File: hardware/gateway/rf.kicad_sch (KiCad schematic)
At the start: 2 parts, among them IC2 CC1101RGPR

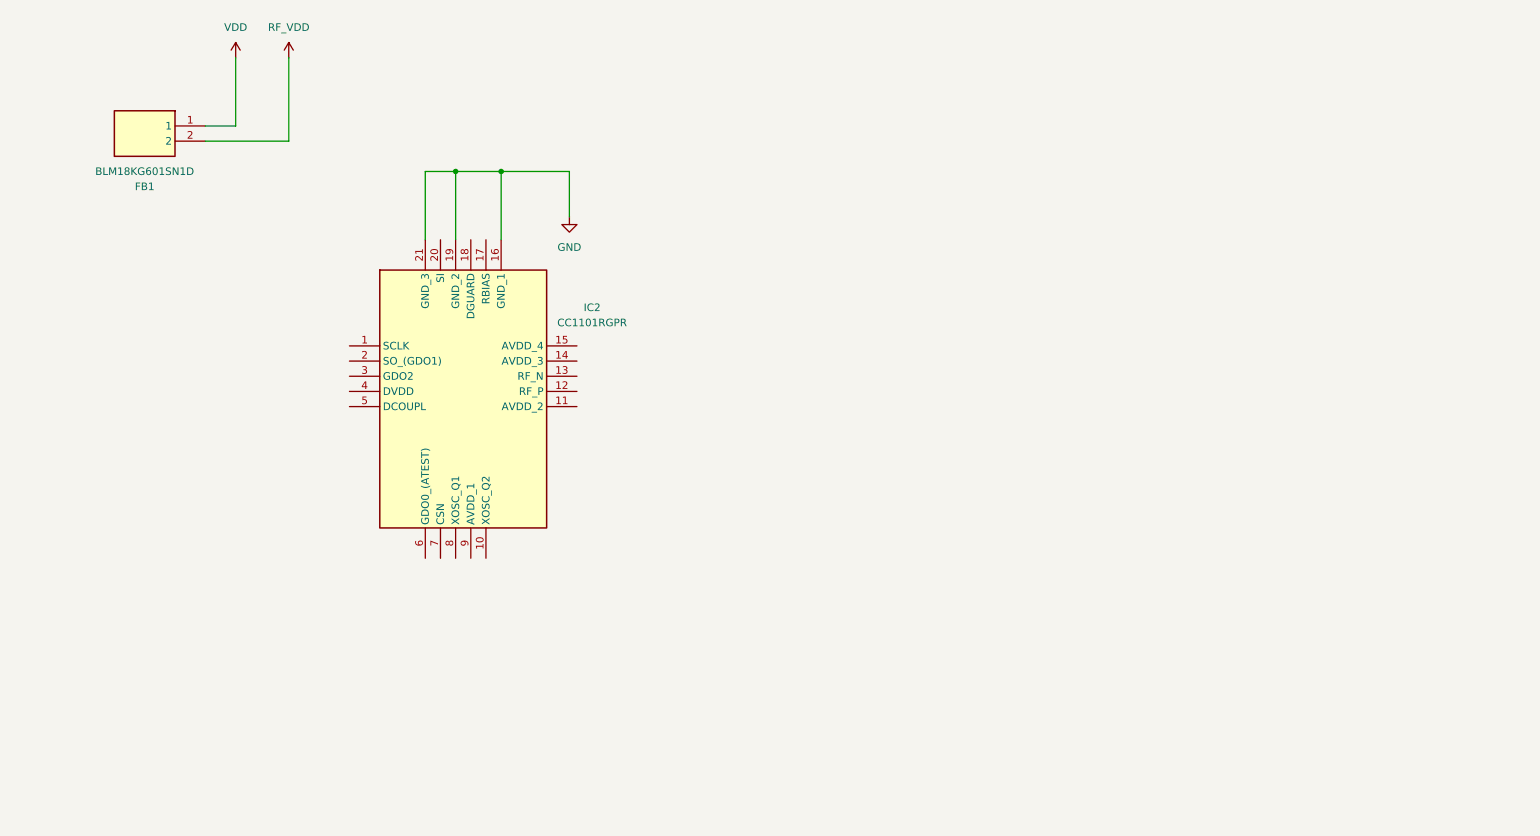
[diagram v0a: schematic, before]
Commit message: EG-11 All components connected in all sheets. The MCU pin mapping needs to be fixed. The BOM needs to be created. The FRAM need needs to be assessed.
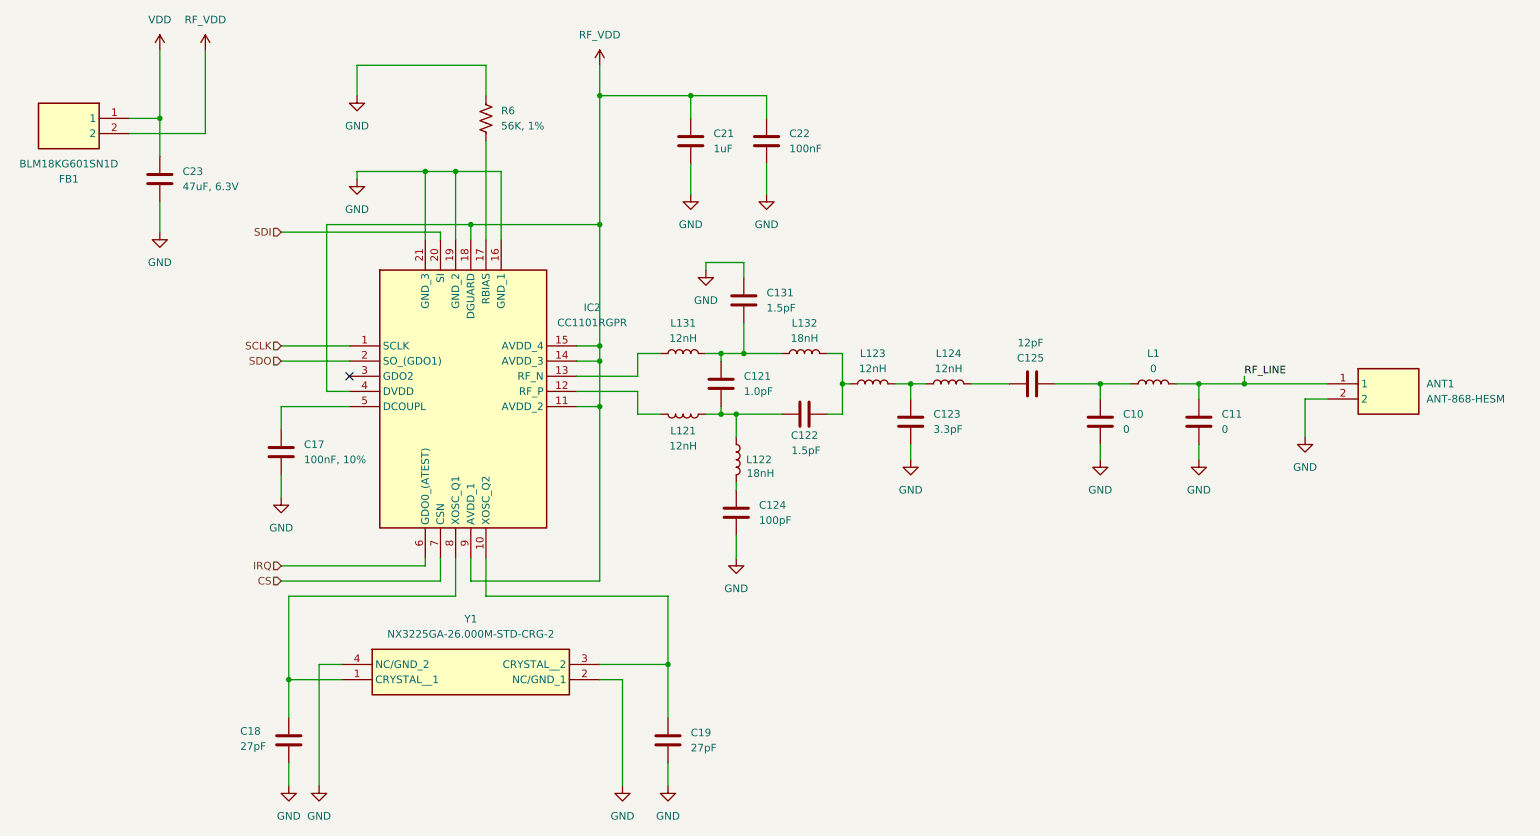
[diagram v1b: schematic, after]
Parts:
- added ANT1: ANT-868-HESM, MyParts:ANT-868-HESM, symbol ANT-868-HESM:ANT-868-HESM
- added C10, C11: 0, symbol Device:C
- added C121: 1.0pF, symbol Device:C
- added C122, C131: 1.5pF, symbol Device:C
- added C123: 3.3pF, symbol Device:C
- added C124: 100pF, symbol Device:C
- added C125: 12pF, symbol Device:C
- added C17: 100nF, 10%, symbol Device:C
- added C18, C19: 27pF, symbol Device:C
- added C21: 1uF, Capacitor_SMD:C_0603_1608Metric, symbol Device:C
- added C22: 100nF, Capacitor_SMD:C_0603_1608Metric, symbol Device:C
- added C23: 47uF, 6.3V, Capacitor_SMD:C_1206_3216Metric, symbol Device:C
- added L1: 0, symbol Device:L
- added L121, L123, L124, L131: 12nH, symbol Device:L
- added L122, L132: 18nH, symbol Device:L
- added R6: 56K, 1%, symbol Device:R_US
- added Y1: NX3225GA-26.000M-STD-CRG-2, MyParts:NX3225GA26000MSTDCRG2, symbol NX3225GA-26_000M-STD-CRG-2:NX3225GA-26.000M-STD-CRG-2
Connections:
- net GND: now also ANT1.2, C10.2, C11.2, C123.2, C124.2, C131.1, C17.2, C18.2, C19.2, C21.2, C22.2, C23.2, R6.1, Y1.2 (NC/GND_1), Y1.4 (NC/GND_2)
- net RF_VDD: now also IC2.11 (AVDD_2), IC2.14 (AVDD_3), IC2.15 (AVDD_4), IC2.18 (DGUARD), IC2.4 (DVDD), IC2.9 (AVDD_1), C21.1, C22.1
- net VDD: now also C23.1
- net SCLK: now reaches IC2.1 (SCLK)
- net at IC2.10 (XOSC_Q2): now also C19.1, Y1.3 (CRYSTAL__2)
- net at IC2.12 (RF_P): now also L121.2
- net at IC2.13 (RF_N): now also L131.1
- net at IC2.17 (RBIAS): now also R6.2
- net SDO: now reaches IC2.2 (SO_(GDO1))
- net SDI: now reaches IC2.20 (SI)
- net at IC2.5 (DCOUPL): now also C17.1
- net IRQ: now reaches IC2.6 (GDO0_(ATEST))
- net CS: now reaches IC2.7 (CSN)
- net at IC2.8 (XOSC_Q1): now also C18.1, Y1.1 (CRYSTAL__1)
- new net: C121.1, C131.2, L131.2, L132.1
- new net: C10.1, C125.2, L1.1
- new net: C121.2, C122.1, L121.1, L122.1
- new net: C123.1, L123.2, L124.1
- new net: C125.1, L124.2
- new net: C124.1, L122.2
- new net: C122.2, L123.1, L132.2
- new net RF_LINE: ANT1.1, C11.1, L1.2
- no-connect marks 0 -> 1
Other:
- moved on the sheet: FB1

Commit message: EG-11 BOM generated.
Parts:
- removed C17: 100nF, 10%, symbol Device:C
- removed C18, C19: 27pF, symbol Device:C
- removed C21: 1uF, Capacitor_SMD:C_0603_1608Metric, symbol Device:C
- removed C22: 100nF, Capacitor_SMD:C_0603_1608Metric, symbol Device:C
- removed C23: 47uF, 6.3V, Capacitor_SMD:C_1206_3216Metric, symbol Device:C
- removed L1: 0, symbol Device:L
- removed R6: 56K, 1%, symbol Device:R_US
- added C10: 1uF, Capacitor_SMD:C_0603_1608Metric, symbol Device:C
- added C11, C12: 100nF, Capacitor_SMD:C_0603_1608Metric, symbol Device:C
- added C13, C14: 12pF, Capacitor_SMD:C_0402_1005Metric, symbol Device:C
- added C9: 47uF, 6.3V, Capacitor_SMD:C_1206_3216Metric, symbol Device:C
- added R13: 56K, Resistor_SMD:R_0402_1005Metric, symbol Device:R_US
- added R14: 0R, Resistor_SMD:R_0603_1608Metric, symbol Device:R_US
- C121: value 1.0pF -> 1pF; footprint (none) -> Capacitor_SMD:C_0402_1005Metric; Manufacturer_Name (none) -> Murata; Manufacturer_Part_Number (none) -> GRM1555C1H1R0BA01J; Mouser Part Number (none) -> 81-GRM1555C1H1R0BA1J; Mouser Price/Stock (none) -> https://pt.mouser.com/ProductDetail/Murata-Electronics/GRM1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
- C122, C131: footprint (none) -> Capacitor_SMD:C_0402_1005Metric; Manufacturer_Name (none) -> Murata; Manufacturer_Part_Number (none) -> GRM1555C1E1R5BA01D; Mouser Part Number (none) -> 81-GRM1555C1E1R5BA1D; Mouser Price/Stock (none) -> https://pt.mouser.com/ProductDetail/Murata-Electronics/GRM1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
- C123: footprint (none) -> Capacitor_SMD:C_0402_1005Metric; Manufacturer_Name (none) -> Murata; Manufacturer_Part_Number (none) -> GRM1555C1H3R3WA01D; Mouser Part Number (none) -> 81-GRM1555C1H3R3WA1D; Mouser Price/Stock (none) -> https://pt.mouser.com/ProductDetail/Murata-Electronics/GRM1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
- C124: footprint (none) -> Capacitor_SMD:C_0402_1005Metric; Manufacturer_Name (none) -> Murata; Manufacturer_Part_Number (none) -> GRM1555C1H101FA01J; Mouser Part Number (none) -> 81-GRM1555C1H101FA1J; Mouser Price/Stock (none) -> https://pt.mouser.com/ProductDetail/Murata-Electronics/GRM1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
- C125: footprint (none) -> Capacitor_SMD:C_0402_1005Metric; Manufacturer_Name (none) -> Murata; Manufacturer_Part_Number (none) -> GRM1555C1H120FA01D; Mouser Part Number (none) -> 81-GRM1555C1H120FA1D; Mouser Price/Stock (none) -> https://pt.mouser.com/ProductDetail/Murata-Electronics/GRM1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
- Csh1: renamed from C10; footprint (none) -> Capacitor_SMD:C_0603_1608Metric
- Csh2: renamed from C11; footprint (none) -> Capacitor_SMD:C_0603_1608Metric
- L121, L123, L124, L131: footprint (none) -> Capacitor_SMD:C_0402_1005Metric; Manufacturer_Name (none) -> Murata; Manufacturer_Part_Number (none) -> LQW15AN12NJ80D; Mouser Part Number (none) -> 81-LQW15AN12NJ80D; Mouser Price/Stock (none) -> https://pt.mouser.com/ProductDetail/Murata-Electronics/LQW1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
- L122, L132: footprint (none) -> Capacitor_SMD:C_0402_1005Metric; Manufacturer_Name (none) -> Murata; Manufacturer_Part_Number (none) -> LQG15HH18NJ02D; Mouser Part Number (none) -> 81-LQG15HH18NJ02D; Mouser Price/Stock (none) -> https://pt.mouser.com/ProductDetail/Murata-Electronics/LQG1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
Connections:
- net GND: now also C123.1, C124.1, C131.2, C10.2, C11.2, C12.2, C13.2, C14.2, C9.2, R13.2; no longer C123.2, C124.2, C131.1
- net RF_LINE: now also R14.2
- net RF_VDD: now also C10.1, C11.1
- net VDD: now also C9.1
- net at L131.2, L132.1: now also C121.2, C131.1; no longer C121.1, C131.2
- net at IC2.17 (RBIAS): now also R13.1
- net at C125.2, Csh1.1: now also R14.1
- net at C122.1, L122.1: now also C121.1, L121.2; no longer C121.2, L121.1
- net at IC2.12 (RF_P): now also L121.1; no longer L121.2
- net at IC2.5 (DCOUPL): now also C12.1
- net at L123.2, L124.1: now also C123.2; no longer C123.1
- net at IC2.10 (XOSC_Q2), Y1.3 (CRYSTAL__2): now also C14.1
- net at IC2.8 (XOSC_Q1), Y1.1 (CRYSTAL__1): now also C13.1
- net at L122.2: now also C124.2; no longer C124.1

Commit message: EG-11 ERC passed.
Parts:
- L121, L122, L123, L124, L131, L132: footprint Capacitor_SMD:C_0402_1005Metric -> Inductor_SMD:L_0402_1005Metric
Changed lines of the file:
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@@
 	)
 	(junction
+		(at 55.88 39.37)
+		(diameter 0)
+		(color 0 0 0 0)
+	)
+	(junction
 		(at 121.92 85.09)
 		(diameter 0)
@@
 	(wire
 		(pts
+			(xy 66.04 39.37) (xy 55.88 39.37)
+		)
+		(stroke
+			(width 0)
+			(type default)
+		)
+	)
+	(wire
+		(pts
 			(xy 121.92 33.02) (xy 121.92 54.61)
 		)
@@
 	(wire
 		(pts
+			(xy 66.04 25.4) (xy 66.04 39.37)
+		)
+		(stroke
+			(width 0)
+			(type default)
+		)
+	)
+	(wire
+		(pts
 			(xy 133.35 116.84) (xy 102.87 116.84)
 		)
@@
 			)
 		)
-		(property "Footprint" "Capacitor_SMD:C_0402_1005Metric"
+		(property "Footprint" "Inductor_SMD:L_0402_1005Metric"
 			(at 135.89 76.2 0)
 			(effects
@@
 			)
 		)
-		(property "Footprint" "Capacitor_SMD:C_0402_1005Metric"
+		(property "Footprint" "Inductor_SMD:L_0402_1005Metric"
 			(at 135.89 86.36 0)
 			(effects
@@
 			)
 		)
-		(property "Footprint" "Capacitor_SMD:C_0402_1005Metric"
+		(property "Footprint" "Inductor_SMD:L_0402_1005Metric"
 			(at 167.64 81.28 0)
 			(effects
@@
 			)
 		)
-		(property "Footprint" "Capacitor_SMD:C_0402_1005Metric"
+		(property "Footprint" "Inductor_SMD:L_0402_1005Metric"
 			(at 144.78 93.98 0)
 			(effects
@@
 			)
 		)
-		(property "Footprint" "Capacitor_SMD:C_0402_1005Metric"
+		(property "Footprint" "Inductor_SMD:L_0402_1005Metric"
 			(at 156.21 76.2 0)
 			(effects
@@
 			)
 		)
-		(property "Footprint" "Capacitor_SMD:C_0402_1005Metric"
+		(property "Footprint" "Inductor_SMD:L_0402_1005Metric"
 			(at 180.34 81.28 0)
 			(effects
@@
 					(unit 1)
 				)
+			)
+		)
+	)
+	(symbol
+		(lib_id "power:PWR_FLAG")
+		(at 66.04 25.4 0)
+		(unit 1)
+		(exclude_from_sim no)
+		(in_bom yes)
+		(on_board yes)
+		(dnp no)
+		(fields_autoplaced yes)
+		(property "Reference" "#FLG04"
+			(at 66.04 23.495 0)
+			(effects
+				(font
+					(size 1.27 1.27)
+				)
+				(hide yes)
+			)
+		)
+		(property "Value" "PWR_FLAG"
+			(at 66.04 20.32 0)
+			(effects
+				(font
+					(size 1.27 1.27)
+				)
+			)
+		)
+		(property "Footprint" ""
+			(at 66.04 25.4 0)
+			(effects
+				(font
+					(size 1.27 1.27)
+				)
+				(hide yes)
+			)
+		)
+		(property "Datasheet" "~"
+			(at 66.04 25.4 0)
+			(effects
+				(font
+					(size 1.27 1.27)
+				)
+				(hide yes)
+			)
+		)
+		(property "Description" "Special symbol for telling ERC where power comes from"
+			(at 66.04 25.4 0)
+			(effects
+				(font
+					(size 1.27 1.27)
+				)
+				(hide yes)
+			)
+		)
+		(pin "1"
+		)
+		(instances
+			(project ""
+				(path "/d3cb7130-decc-418b-958e-e5d84a8d867f/af07603d-259f-481d-be2c-d925e27835a3"
+					(reference "#FLG04")
+					(unit 1)
+				)

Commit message: EG-12 Components placed without connections. Balun components place needs to be fixed.
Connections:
- net GND: no longer ANT1.2
- no-connect marks 1 -> 2
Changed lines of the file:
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@@
 		(at 80.01 80.01)
 	)
+	(no_connect
+		(at 243.84 83.82)
+	)
 	(wire
 		(pts
@@
 	(wire
 		(pts
-			(xy 240.03 90.17) (xy 240.03 83.82)
-		)
-		(stroke
-			(width 0)
-			(type default)
-		)
-	)
-	(wire
-		(pts
 			(xy 171.45 81.28) (xy 173.99 81.28)
 		)
@@
 	(wire
 		(pts
-			(xy 240.03 83.82) (xy 243.84 83.82)
-		)
-		(stroke
-			(width 0)
-			(type default)
-		)
-	)
-	(wire
-		(pts
 			(xy 92.71 111.76) (xy 92.71 110.49)
 		)
@@
 					(unit 1)
 				)
-			)
-		)
-	)
-	(symbol
-		(lib_id "power:GND")
-		(at 240.03 90.17 0)
-		(unit 1)
-		(exclude_from_sim no)
-		(in_bom yes)
-		(on_board yes)
-		(dnp no)
-		(fields_autoplaced yes)
-		(property "Reference" "#PWR051"
-			(at 240.03 96.52 0)
-			(effects
-				(font
-					(size 1.27 1.27)
-				)
-				(hide yes)
-			)
-		)
-		(property "Value" "GND"
-			(at 240.03 95.25 0)
-			(effects
-				(font
-					(size 1.27 1.27)
-				)
-			)
-		)
-		(property "Footprint" ""
-			(at 240.03 90.17 0)
-			(effects
-				(font
-					(size 1.27 1.27)
-				)
-				(hide yes)
-			)
-		)
-		(property "Datasheet" ""
-			(at 240.03 90.17 0)
-			(effects
-				(font
-					(size 1.27 1.27)
-				)
-				(hide yes)
-			)
-		)
-		(property "Description" "Power symbol creates a global label with name \"GND\" , ground"
-			(at 240.03 90.17 0)
-			(effects
-				(font
-					(size 1.27 1.27)
-				)
-				(hide yes)
-			)
-		)
-		(pin "1"
-		)
-		(instances
-			(project "gateway"
-				(path "/d3cb7130-decc-418b-958e-e5d84a8d867f/af07603d-259f-481d-be2c-d925e27835a3"
-					(reference "#PWR051")
-					(unit 1)
-				)

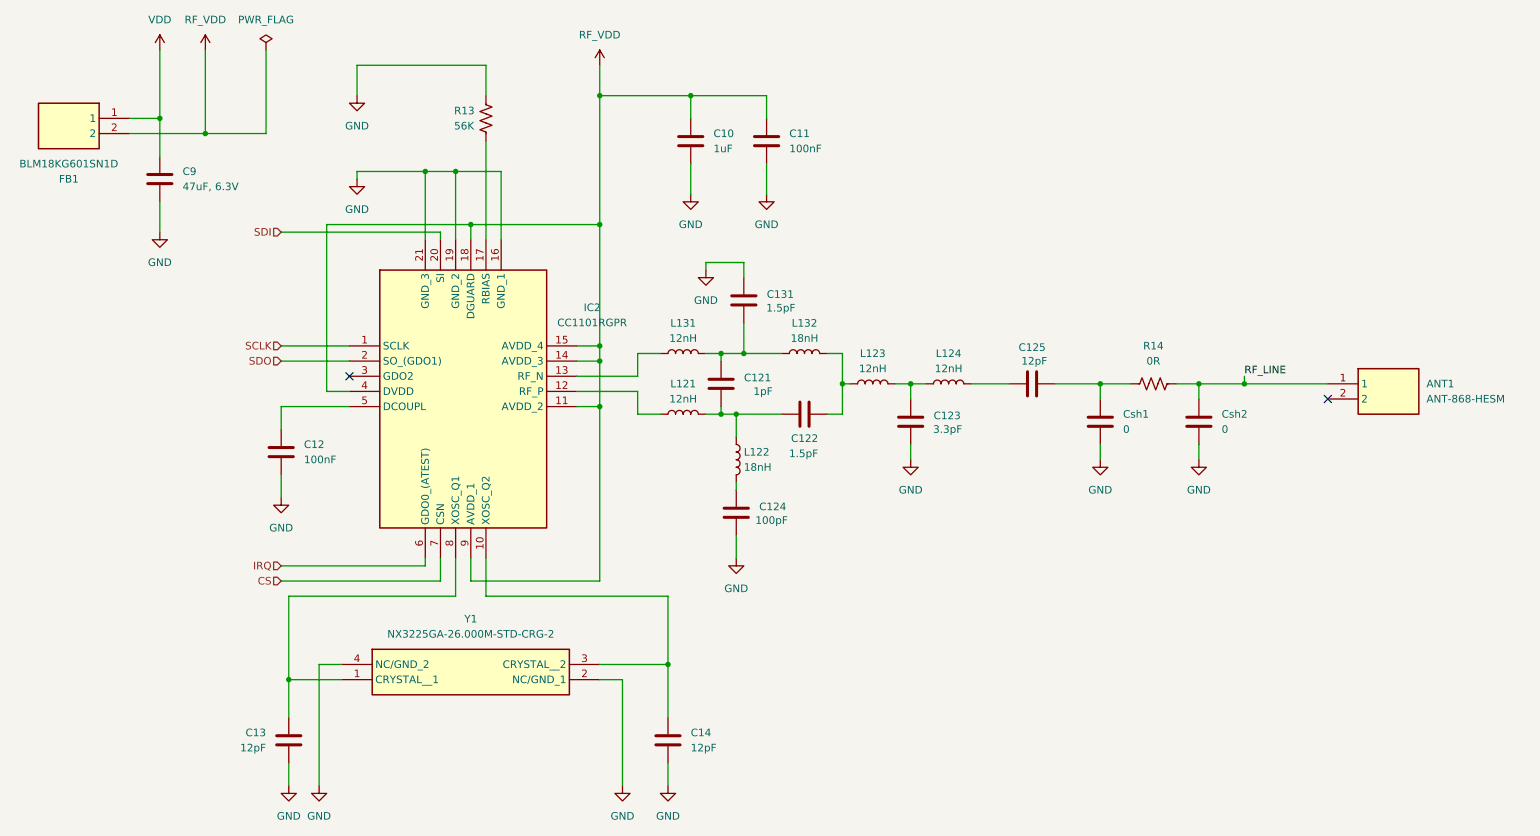
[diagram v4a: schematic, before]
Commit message: EG-12 All components placed. RF connected, except antenna. Buzzer connected, buzzer power supply connected, FRAM connected. Majority os MCU connections  missing.
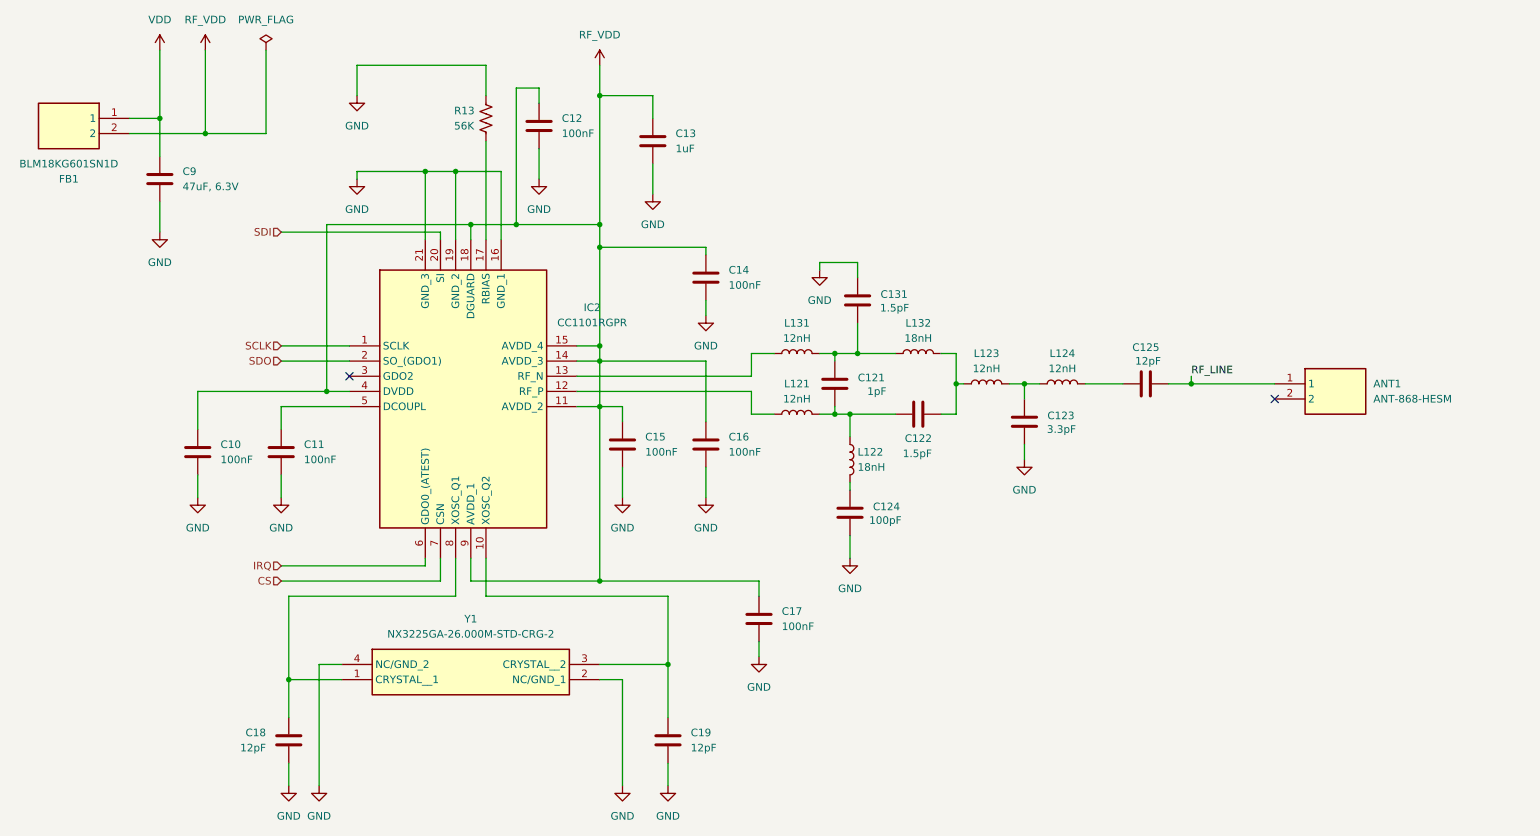
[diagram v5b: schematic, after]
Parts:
- removed Csh1, Csh2: 0, Capacitor_SMD:C_0603_1608Metric, symbol Device:C
- removed R14: 0R, Resistor_SMD:R_0603_1608Metric, symbol Device:R_US
- added C13: 1uF, Capacitor_SMD:C_0402_1005Metric, symbol Device:C
- added C14, C15, C16, C17: 100nF, Capacitor_SMD:C_0402_1005Metric, symbol Device:C
- C10: value 1uF -> 100nF; footprint Capacitor_SMD:C_0603_1608Metric -> Capacitor_SMD:C_0402_1005Metric; Manufacturer_Name TAYO YUDEN -> Yageo; Manufacturer_Part_Number MBASE168SB7105KTNA18 -> CC0402KRX7R7BB104; Mouser Part Number 963-MBASE168SB7105KT -> 603-CC402KRX7R7BB104; Mouser Price/Stock https://pt.mouser.com/ProductDetail/TAIYO-YUDEN/MBASE168SB7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 -> https://pt.mouser.com/ProductDetail/YAGEO/CC0402KRX7R7BB104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
- C11, C12: footprint Capacitor_SMD:C_0603_1608Metric -> Capacitor_SMD:C_0402_1005Metric; Manufacturer_Name Murata -> Yageo; Manufacturer_Part_Number GCJ188R72A104KA1D -> CC0402KRX7R7BB104; Mouser Part Number 81-GCJ188R72A104KA1D -> 603-CC402KRX7R7BB104; Mouser Price/Stock https://pt.mouser.com/ProductDetail/Murata-Electronics/GCJ1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 -> https://pt.mouser.com/ProductDetail/YAGEO/CC0402KRX7R7BB104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
- renumbered C13 to C18, C14 to C19
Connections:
- net GND: now also C13.2, C14.2, C15.2, C16.2, C17.2
- net RF_LINE: now also C125.2
- net RF_VDD: now also C12.1, C13.1, C14.1, C15.1, C16.1, C17.1; no longer C11.1
- net at IC2.5 (DCOUPL): now also C11.1; no longer C12.1
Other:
- moved on the sheet: ANT1, C121, C122, C123, C124, C125, C131, L121, L122, L123, L124, L131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
